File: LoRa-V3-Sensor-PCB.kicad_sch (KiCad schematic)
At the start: 6 parts, among them IC1 BME690, IC2 SHT40-BD1B-R2, IC3 TSL25911FN

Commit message: improve workflow
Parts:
- C1, C2: genericPartNumber GPC0603104-25-X7R -> (none)
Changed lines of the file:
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@@
 			)
 		)
-		(property "genericPartNumber" "GPC0603104-25-X7R"
+		(property "genericPartNumber" ""
 			(at 194.31 111.76 0)
 			(effects
@@
 			)
 		)
-		(property "genericPartNumber" "GPC0603104-25-X7R"
+		(property "genericPartNumber" ""
 			(at 111.76 109.22 0)
 			(effects

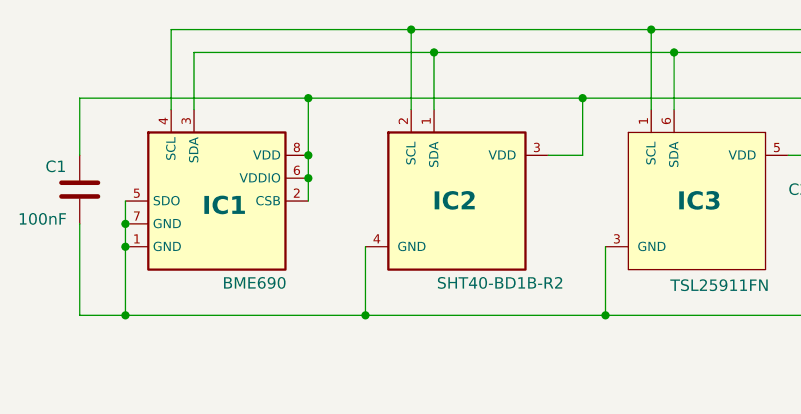
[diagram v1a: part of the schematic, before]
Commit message: split release into a separate workflow
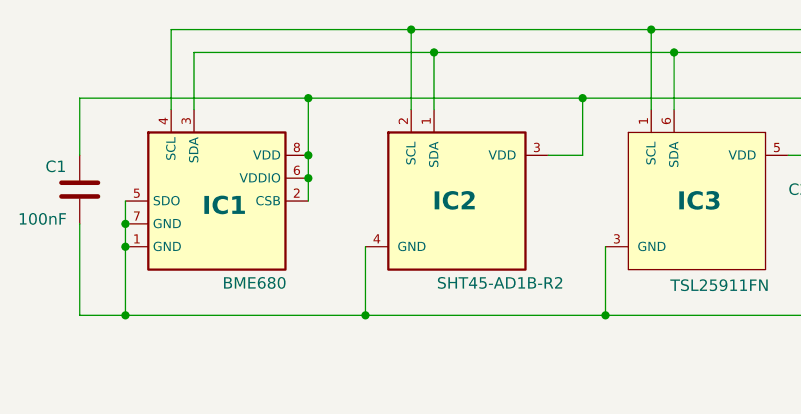
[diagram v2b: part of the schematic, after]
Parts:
- IC1: value BME690 -> BME680; manufacturerPartNumber BME690 -> BME680
- IC2: value SHT40-BD1B-R2 -> SHT45-AD1B-R2; manufacturerPartNumber SHT40-BD1B-R2 -> SHT45-AD1B-R2
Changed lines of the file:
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@@
 			)
 		)
-		(property "Value" "SHT40-BD1B-R2"
+		(property "Value" "SHT45-AD1B-R2"
 			(at 158.496 119.634 0)
 			(effects
@@
 			)
 		)
-		(property "manufacturerPartNumber" "SHT40-BD1B-R2"
+		(property "manufacturerPartNumber" "SHT45-AD1B-R2"
 			(at 153.67 133.35 0)
 			(effects
@@
 			)
 		)
-		(property "Value" "BME690"
+		(property "Value" "BME680"
 			(at 134.747 119.634 0)
 			(effects
@@
 			)
 		)
-		(property "manufacturerPartNumber" "BME690"
+		(property "manufacturerPartNumber" "BME680"
 			(at 127 64.77 0)
 			(effects

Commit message: add mpn as field
this is required as Aisler needs this specific field name and cannot read the already existing manufacturerPartNumber field
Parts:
- C1, C2: mpn (none) -> CGA3E2X7R1E104K080AA
- CONN1: mpn (none) -> BC034-08-A-V-0150-L-C
- IC1: mpn (none) -> BME680
- IC2: mpn (none) -> SHT45-AD1B-R2
- IC3: mpn (none) -> TSL25911FN
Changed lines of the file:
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@@
+			)
+		)
+		(property "mpn" "SHT45-AD1B-R2"
+			(at 153.67 110.49 0)
+			(effects
+				(font
+					(size 1.27 1.27)
+				)
+				(hide yes)
 			)
 		)
@@
 			)
 		)
+		(property "mpn" "CGA3E2X7R1E104K080AA"
+			(at 194.31 111.76 0)
+			(effects
+				(font
+					(size 1.27 1.27)
+				)
+				(hide yes)
+			)
+		)
 		(pin "1"
 		)
@@
 		)
 		(property "manufacturerPartNumber" "CGA3E2X7R1E104K080AA"
+			(at 111.76 109.22 0)
+			(effects
+				(font
+					(size 1.27 1.27)
+				)
+				(hide yes)
+			)
+		)
+		(property "mpn" "CGA3E2X7R1E104K080AA"
 			(at 111.76 109.22 0)
 			(effects
@@
 			)
 		)
+		(property "mpn" "BC034-08-A-V-0150-L-C"
+			(at 248.92 104.14 0)
+			(effects
+				(font
+					(size 1.27 1.27)
+				)
+				(hide yes)
+			)
+		)
 		(pin "1"
 		)
@@
 			)
 		)
+		(property "mpn" "TSL25911FN"
+			(at 180.34 110.49 0)
+			(effects
+				(font
+					(size 1.27 1.27)
+				)
+				(hide yes)
+			)
+		)
 		(pin "6"
 		)
@@
 			(effects
 				(font
+					(size 1.27 1.27)
+				)
+				(hide yes)
+			)
+		)
+		(property "mpn" "BME680"
+			(at 127 110.49 0)
+			(effects
+				(font
